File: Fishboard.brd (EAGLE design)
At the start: 43 x 68 mm, 26 parts, among them J3 B1, J4 B2, J5 B3, J7 B4, Q1 FQP30N06L, Q2 FQP30N06L

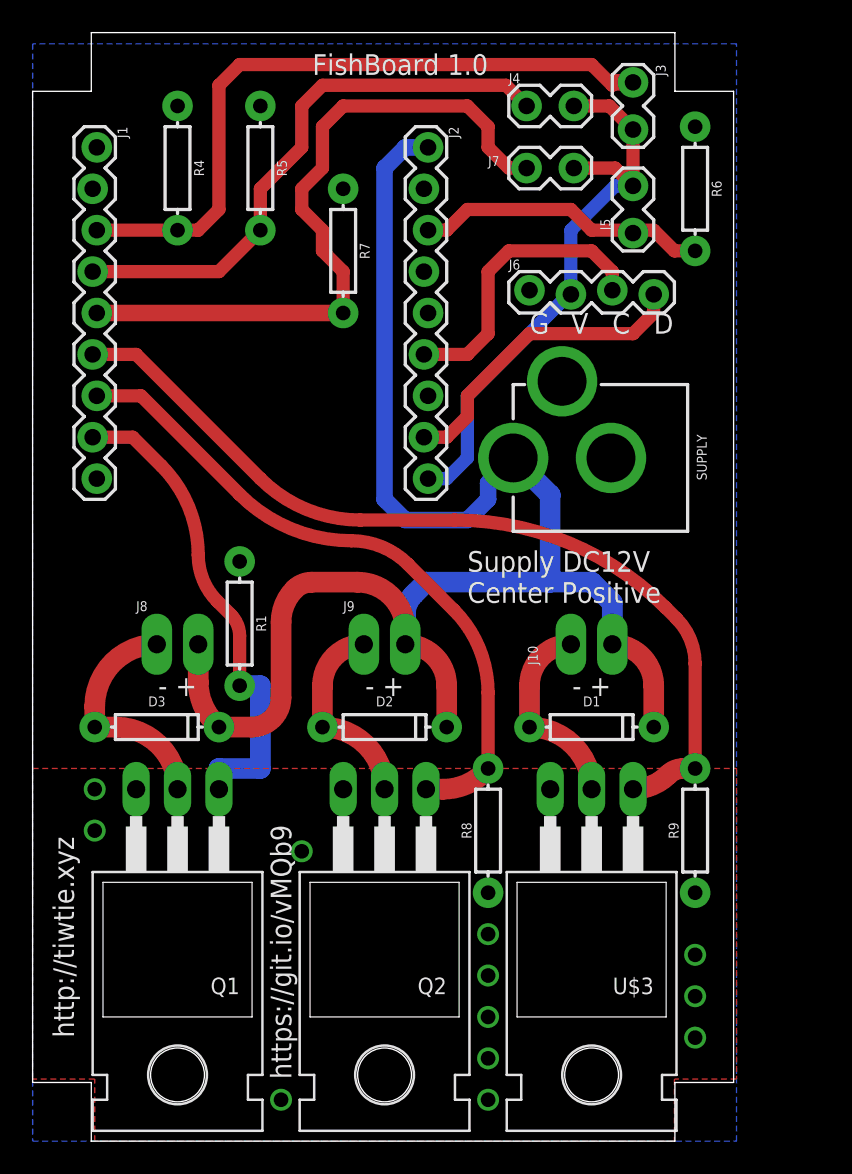
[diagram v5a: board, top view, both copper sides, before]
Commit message: Change the net for the gndplane-connecting vias to GND. Renamed a FET to Q3 instead of U$3.
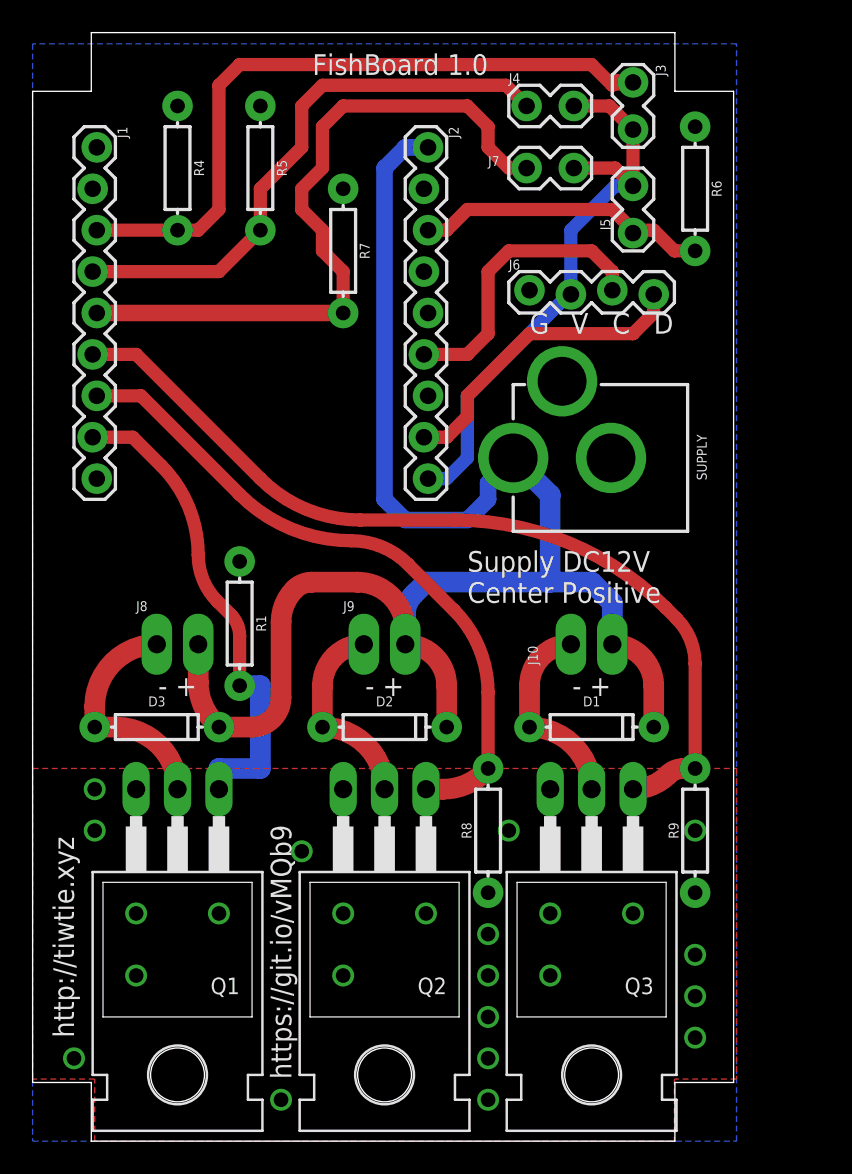
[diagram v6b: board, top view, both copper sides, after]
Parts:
- renumbered U$3 to Q3
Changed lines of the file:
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@@
 <element name="Q1" library="fishlib" package="TO220" value="FQP30N06L" x="8.89" y="15.24" rot="R180"/>
 <element name="Q2" library="fishlib" package="TO220" value="FQP30N06L" x="21.59" y="15.24" rot="R180"/>
-<element name="U$3" library="fishlib" package="TO220" value="FQP30N06L" x="34.29" y="15.24" rot="R180"/>
+<element name="Q3" library="fishlib" package="TO220" value="FQP30N06L" x="34.29" y="15.24" rot="R180"/>
 <element name="D1" library="SparkFun-DiscreteSemi" package="DIODE-1N4148-KIT" value="200mA/100V/1V" x="34.29" y="25.4">
 <attribute name="PROD_ID" value="DIO-08378" x="34.29" y="25.4" size="1.778" layer="27" display="off"/>
@@
 <contactref element="Q1" pad="S"/>
 <contactref element="Q2" pad="S"/>
-<contactref element="U$3" pad="S"/>
+<contactref element="Q3" pad="S"/>
 <polygon width="0.8128" layer="1">
 <vertex x="0" y="22.86"/>
@@
 <vertex x="0" y="3.81"/>
 </polygon>
+<via x="16.51" y="17.78" extent="1-16" drill="0.9"/>
+<via x="3.81" y="19.05" extent="1-16" drill="0.9"/>
+<via x="3.81" y="21.59" extent="1-16" drill="0.9"/>
+<via x="27.94" y="12.7" extent="1-16" drill="0.9"/>
+<via x="27.94" y="10.16" extent="1-16" drill="0.9"/>
+<via x="27.94" y="7.62" extent="1-16" drill="0.9"/>
+<via x="27.94" y="5.08" extent="1-16" drill="0.9"/>
+<via x="40.64" y="11.43" extent="1-16" drill="0.9"/>
+<via x="40.64" y="8.89" extent="1-16" drill="0.9"/>
+<via x="40.64" y="6.35" extent="1-16" drill="0.9"/>
+<via x="2.54" y="5.08" extent="1-16" drill="0.9"/>
+<via x="29.21" y="19.05" extent="1-16" drill="0.9"/>
+<via x="40.64" y="19.05" extent="1-16" drill="0.9"/>
+<via x="6.35" y="13.97" extent="1-16" drill="0.9"/>
+<via x="6.35" y="10.16" extent="1-16" drill="0.9"/>
+<via x="11.43" y="13.97" extent="1-16" drill="0.9"/>
+<via x="19.05" y="13.97" extent="1-16" drill="0.9"/>
+<via x="24.13" y="13.97" extent="1-16" drill="0.9"/>
+<via x="19.05" y="10.16" extent="1-16" drill="0.9"/>
+<via x="36.83" y="13.97" extent="1-16" drill="0.9"/>
+<via x="31.75" y="13.97" extent="1-16" drill="0.9"/>
+<via x="31.75" y="10.16" extent="1-16" drill="0.9"/>
+<via x="15.24" y="2.54" extent="1-16" drill="0.9"/>
+<via x="27.94" y="2.54" extent="1-16" drill="0.9"/>
 </signal>
 <signal name="VCC12">
@@
 <contactref element="J1" pad="6"/>
 <contactref element="R9" pad="P$2"/>
-<contactref element="U$3" pad="G"/>
+<contactref element="Q3" pad="G"/>
 <wire x1="36.83" y1="21.59" x2="38.998025" y2="22.488025" width="1.27" layer="1" curve="45"/>
 <wire x1="38.998025" y1="22.488025" x2="39.896053125" y2="22.86" width="1.27" layer="1" curve="-45"/>
@@
 <wire x1="24.257" y1="55.88" x2="25.4" y2="55.88" width="0.8128" layer="1"/>
 <wire x1="25.4" y1="55.88" x2="26.67" y2="57.15" width="0.8128" layer="1"/>
-<wire x1="26.67" y1="57.15" x2="33.02" y2="57.15" width="0.8128" layer="1"/>
-<wire x1="33.02" y1="57.15" x2="34.29" y2="55.88" width="0.8128" layer="1"/>
-<wire x1="34.29" y1="55.88" x2="36.6522" y2="55.88" width="0.8128" layer="1"/>
+<wire x1="26.67" y1="57.15" x2="35.56" y2="57.15" width="0.8128" layer="1"/>
+<wire x1="35.56" y1="57.15" x2="36.83" y2="55.88" width="0.8128" layer="1"/>
+<wire x1="36.83" y1="55.88" x2="36.6522" y2="55.88" width="0.8128" layer="1"/>
 <wire x1="36.6522" y1="55.88" x2="36.83" y2="55.7022" width="0.8128" layer="1"/>
 <wire x1="40.64" y1="54.61" x2="39.37" y2="54.61" width="0.8128" layer="1"/>
@@
 </signal>
 <signal name="N$4">
-<contactref element="U$3" pad="D"/>
+<contactref element="Q3" pad="D"/>
 <contactref element="J10" pad="1"/>
 <contactref element="D1" pad="A"/>
@@
 <wire x1="30.48" y1="25.4" x2="34.29" y2="21.59" width="1.27" layer="1" curve="-90"/>
 </signal>
-<signal name="N$3">
-<via x="3.81" y="21.59" extent="1-16" drill="0.9"/>
-</signal>
-<signal name="N$5">
-<via x="3.81" y="19.05" extent="1-16" drill="0.9"/>
-</signal>
-<signal name="N$6">
-<via x="15.24" y="2.54" extent="1-16" drill="0.9"/>
-</signal>
-<signal name="N$7">
-<via x="27.94" y="2.54" extent="1-16" drill="0.9"/>
-</signal>
-<signal name="N$8">
-<via x="27.94" y="5.08" extent="1-16" drill="0.9"/>
-</signal>
-<signal name="N$9">
-<via x="27.94" y="7.62" extent="1-16" drill="0.9"/>
-</signal>
-<signal name="N$10">
-<via x="27.94" y="10.16" extent="1-16" drill="0.9"/>
-</signal>
-<signal name="N$11">
-<via x="27.94" y="12.7" extent="1-16" drill="0.9"/>
-</signal>
-<signal name="N$12">
-<via x="40.64" y="6.35" extent="1-16" drill="0.9"/>
-</signal>
-<signal name="N$13">
-<via x="40.64" y="8.89" extent="1-16" drill="0.9"/>
-</signal>
-<signal name="N$14">
-<via x="40.64" y="11.43" extent="1-16" drill="0.9"/>
-</signal>
-<signal name="N$15">
-<via x="16.51" y="17.78" extent="1-16" drill="0.9"/>
-</signal>
 </signals>
